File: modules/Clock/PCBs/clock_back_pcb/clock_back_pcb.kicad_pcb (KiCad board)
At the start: 2 copper layers, 38.1 x 68.6 mm, 7 parts, among them J10 Conn_01x11_Pin, J11 Eurorack_2x8_Power, J9 Conn_01x08_Socket

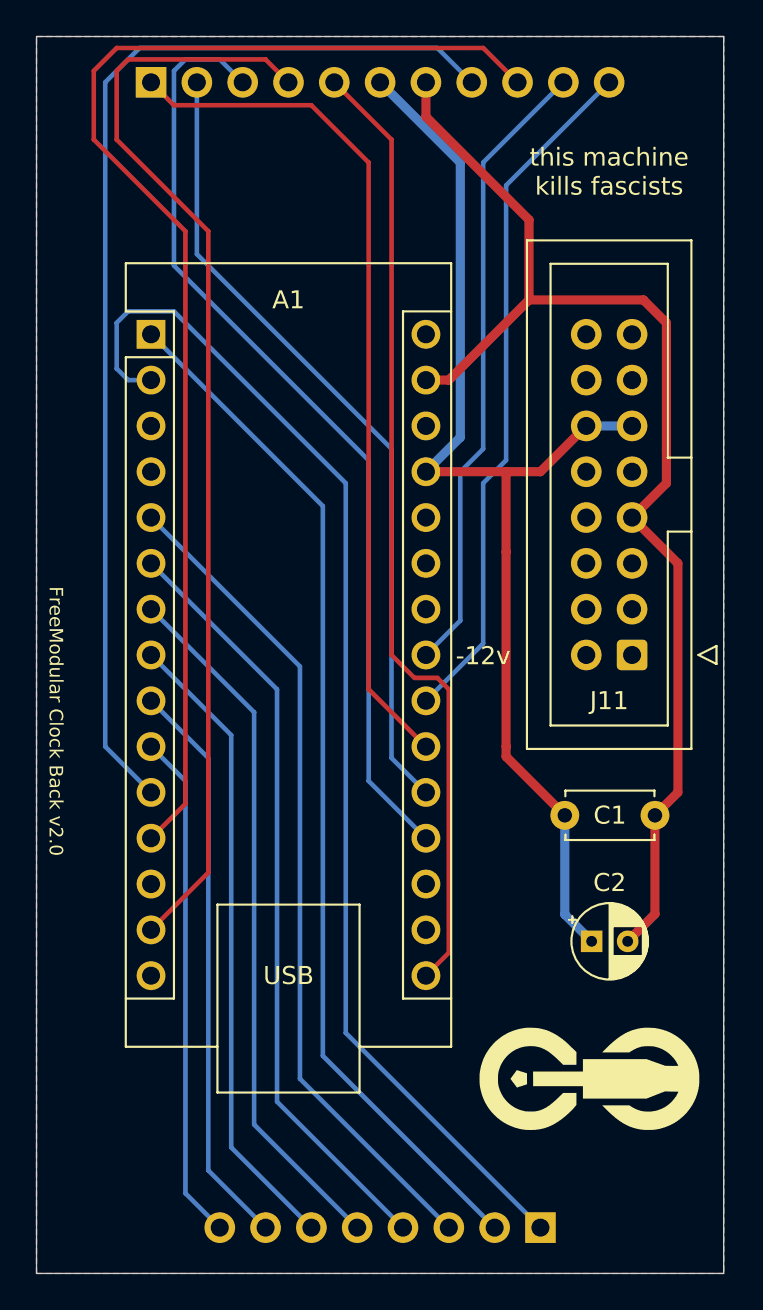
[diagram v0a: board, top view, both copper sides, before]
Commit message: tweak clock faceplate
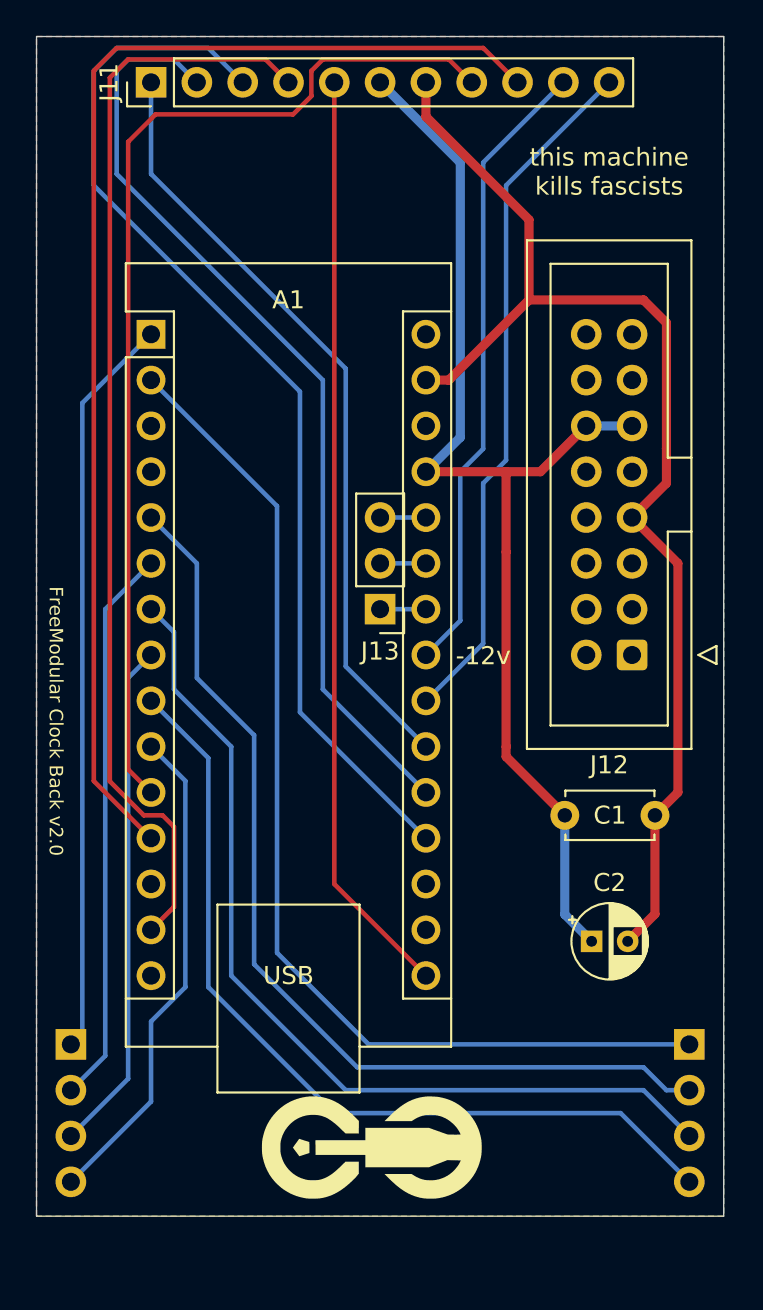
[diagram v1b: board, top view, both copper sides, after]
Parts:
- added J12: Eurorack_2x8_Power, Connector_IDC:IDC-Header_2x08_P2.54mm_Vertical, F.Cu at (58.4, 96.5)
- added J13: Conn_01x03_Socket, Connector_PinHeader_2.54mm:PinHeader_1x03_P2.54mm_Vertical, F.Cu at (44.5, 94.0)
- J10: value Conn_01x11_Pin -> Conn_01x04_Pin; footprint Connector_PinHeader_2.54mm:PinHeader_1x11_P2.54mm_Vertical -> Connector_PinHeader_2.54mm:PinHeader_1x04_P2.54mm_Vertical
- J11: value Eurorack_2x8_Power -> Conn_01x11_Pin; footprint Connector_IDC:IDC-Header_2x08_P2.54mm_Vertical -> Connector_PinHeader_2.54mm:PinHeader_1x11_P2.54mm_Vertical
- J9: value Conn_01x08_Socket -> Conn_01x04_Pin; footprint Connector_PinHeader_2.54mm:PinHeader_1x08_P2.54mm_Vertical -> Connector_PinHeader_2.54mm:PinHeader_1x04_P2.54mm_Vertical
- moved J10 53.5 mm to (27.3, 118.1), turned to 180 degrees
- moved J11 41.5 mm to (31.8, 64.8), turned to 90 degrees
- moved J9 13.1 mm to (61.6, 118.1), turned to 180 degrees
- moved REF** 12.7 mm to (44.5, 123.8)
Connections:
- net Net-(A1-D0/RX) renamed OUT_1
- A1 pad 1: Net-(A1-D1/TX) -> OUT_2
- A1 pad 10: Net-(A1-D7) -> OUT_8
- A1 pad 24: unconnected-(A1-A5-Pad24) -> Net-(A1-A5)
- A1 pad 25: unconnected-(A1-A6-Pad25) -> Net-(A1-A6)
- A1 pad 26: unconnected-(A1-A7-Pad26) -> Net-(A1-A7)
- A1 pad 5: Net-(A1-D2) -> OUT_3
- A1 pad 6: Net-(A1-D3) -> OUT_4
- A1 pad 7: Net-(A1-D4) -> OUT_5
- A1 pad 8: Net-(A1-D5) -> OUT_6
- A1 pad 9: Net-(A1-D6) -> OUT_7
- J10 pad 1: SPI_CS -> OUT_2
- J10 pad 2: SPI_DC -> OUT_4
- J10 pad 3: RESET -> OUT_6
- J10 pad 4: SPI_SDA -> OUT_8
- J11 pad 1: unconnected-(J11--12v-Pad1) -> SPI_CS
- J11 pad 10: unconnected-(J11-+12v-Pad10) -> ENCODER_SWITCH
- J11 pad 11: +5V -> PAUSE_BTN
- J11 pad 2: unconnected-(J11--12v-Pad1) -> SPI_DC
- J11 pad 3: GND -> RESET
- J11 pad 4: GND -> SPI_SDA
- J11 pad 5: GND -> SPI_SCK
- J11 pad 6: GND -> +5V
- J11 pad 8: GND -> ENCODER_A
- J11 pad 9: unconnected-(J11-+12v-Pad10) -> ENCODER_B
- J9 pad 2: Net-(A1-D1/TX) -> OUT_3
- J9 pad 3: Net-(A1-D2) -> OUT_5
- J9 pad 4: Net-(A1-D3) -> OUT_7
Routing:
- net Net-(A1-D1/TX): track 57.4 -> 0.00 mm
- net OUT_3: track 0.00 -> 54.2 mm
- net OUT_5: track 0.00 -> 51.2 mm
- net OUT_7: track 0.00 -> 48.3 mm
- net Net-(A1-D2): track 46.2 -> 0.00 mm
- net Net-(A1-D3): track 42.6 -> 0.00 mm
- net OUT_2: track 0.00 -> 41.2 mm
- net Net-(A1-D4): track 39.0 -> 0.00 mm
- net Net-(A1-D5): track 35.4 -> 0.00 mm
- net Net-(A1-D6): track 31.8 -> 0.00 mm
- net OUT_4: track 0.00 -> 31.1 mm
- net OUT_6: track 0.00 -> 28.5 mm
- net Net-(A1-D7): track 28.2 -> 0.00 mm
- net OUT_8: track 0.00 -> 27.5 mm
- net OUT_1: track 67.4 -> 59.6 mm
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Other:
- board size 38.1 x 68.6 mm -> 38.1 x 65.4 mm

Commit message: update clock BOM
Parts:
- renumbered REF** to G1
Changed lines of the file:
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@@
   (footprint "FreeModualr:logo_small" (layer "F.Cu")
     (at 44.45 123.825)
-    (fp_text reference "REF**" (at 0 -0.5 unlocked) (layer "F.SilkS") hide
+    (fp_text reference "G1" (at 0 -0.5 unlocked) (layer "F.SilkS") hide
         (effects (font (size 1 1) (thickness 0.1)))
     )

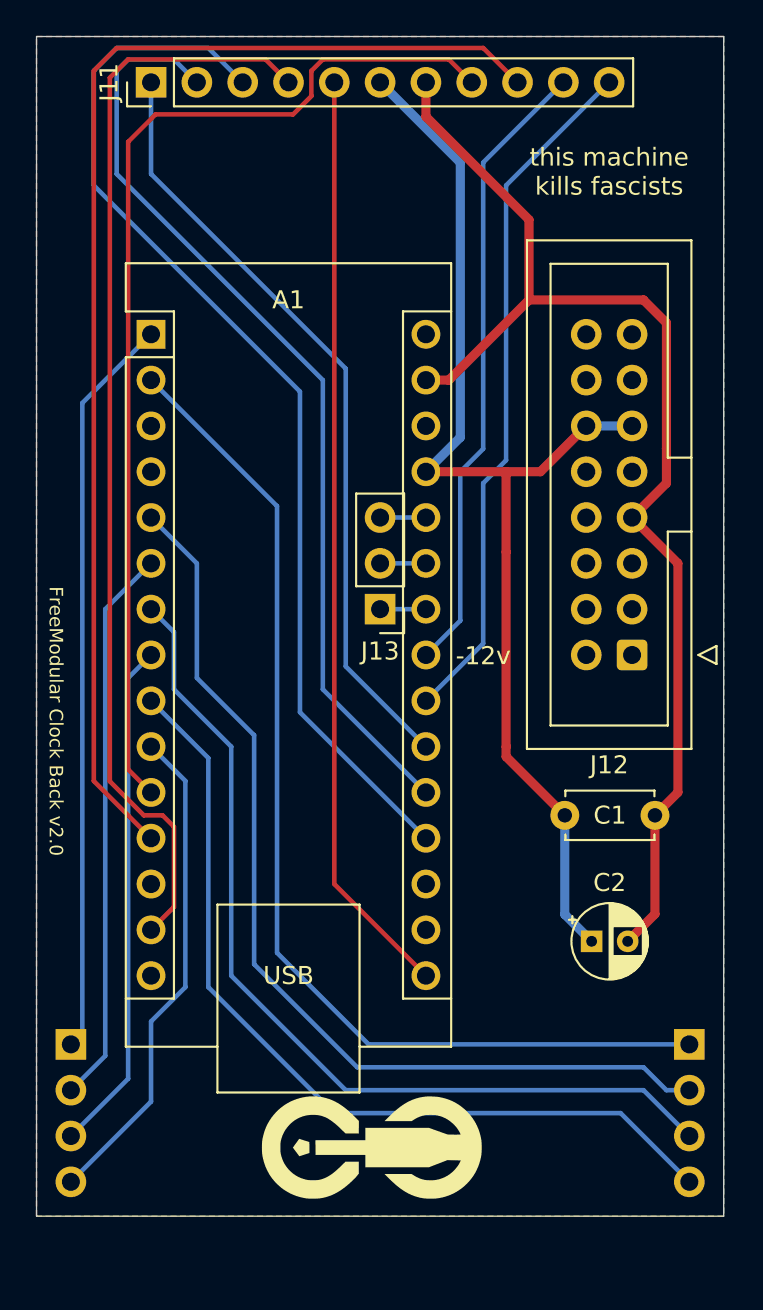
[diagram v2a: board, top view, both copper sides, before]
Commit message: move arduino in clock backpack
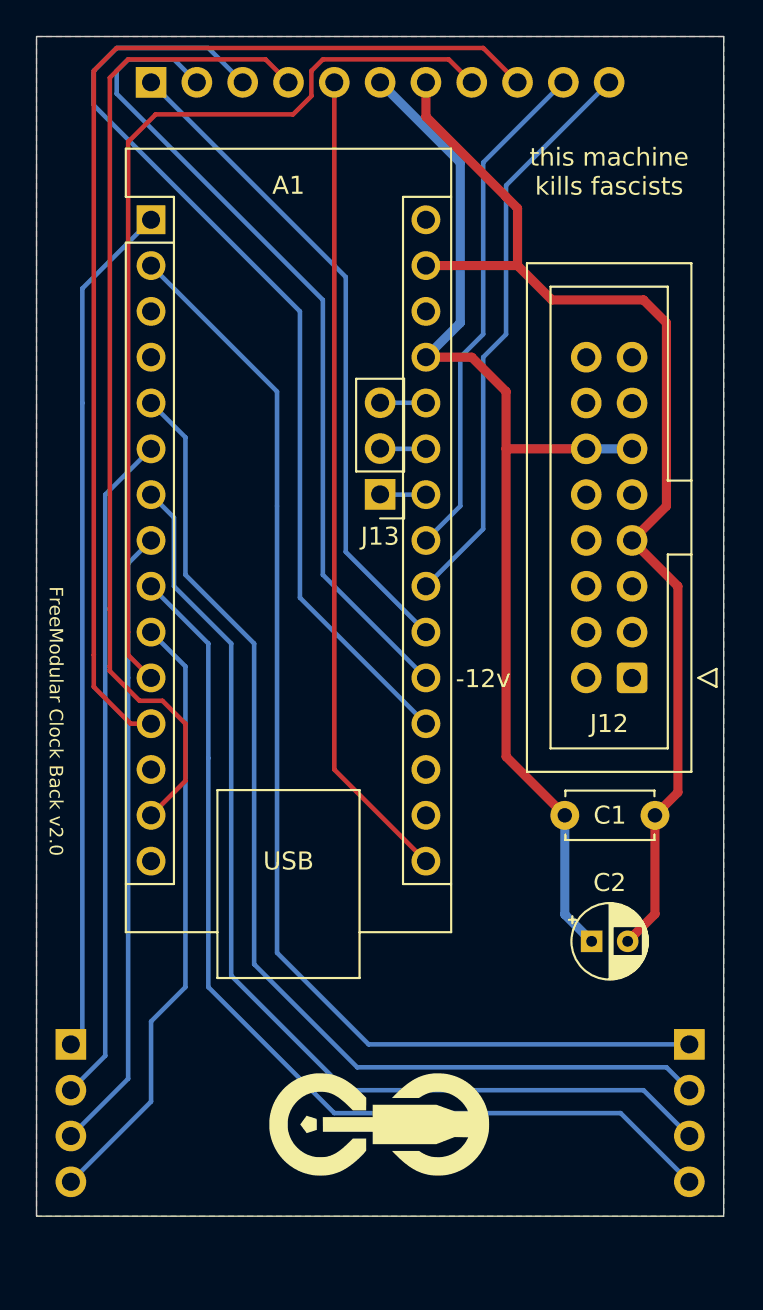
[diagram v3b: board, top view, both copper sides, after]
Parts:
- J11: moved to B.Cu
- moved J13 6.37 mm to (44.5, 87.6)
- moved A1 6.35 mm to (31.8, 72.4)
- moved G1 1.34 mm to (44.9, 122.5)
- moved J12 1.27 mm to (58.4, 97.8)
- turned J11 to -90 degrees
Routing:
- net PAUSE_BTN: track 38.5 -> 32.1 mm
- net RESET: track 59.7 -> 53.4 mm
- net OUT_7: track 48.3 -> 54.7 mm
- net OUT_5: track 51.2 -> 57.6 mm
- net OUT_3: track 54.2 -> 60.5 mm
- net ENCODER_SWITCH: track 34.9 -> 28.6 mm
- net SPI_SCK: track 51.6 -> 45.3 mm
- net SPI_DC: track 52.3 -> 46.0 mm
- net SPI_CS: track 43.1 -> 36.8 mm
- net OUT_8: track 27.5 -> 33.9 mm
- net OUT_6: track 28.5 -> 34.9 mm
- net OUT_4: track 31.1 -> 37.4 mm
- net OUT_2: track 41.2 -> 47.6 mm
- net OUT_1: track 59.6 -> 66.0 mm
- net ENCODER_A: track 58.9 -> 52.5 mm
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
